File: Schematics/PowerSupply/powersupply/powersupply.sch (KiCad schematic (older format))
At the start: 12 parts, among them J1 +/- 15V Regulated, J2 +/- 18V unregulated, T1 Transformer_1P_2S, U1 L7815, U2 L7915

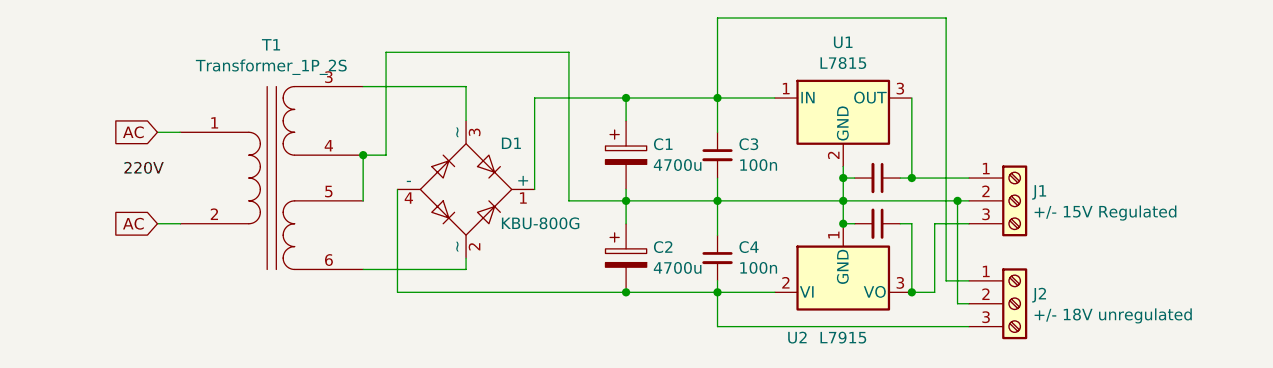
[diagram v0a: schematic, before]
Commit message: Create PCB for the power supply (amp)
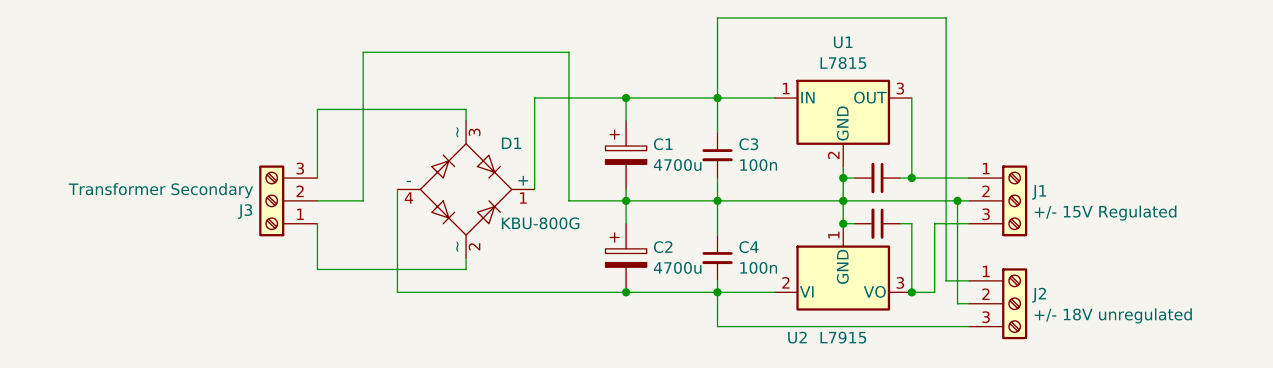
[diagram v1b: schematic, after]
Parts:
- removed T1: Transformer_1P_2S, symbol Device:Transformer_1P_2S
- added J3: Transformer Secondary, TerminalBlock:TerminalBlock_Altech_AK300-3_P5.00mm, symbol Connector:Screw_Terminal_01x03
- C1, C2: footprint (none) -> Capacitor_THT:CP_Radial_D10.0mm_P5.00mm
- C3, C4, C5, C6: footprint (none) -> Capacitor_THT:C_Rect_L4.0mm_W2.5mm_P2.50mm
- J1, J2: footprint (none) -> TerminalBlock:TerminalBlock_Altech_AK300-3_P5.00mm
- U1, U2: footprint (none) -> Package_TO_SOT_THT:TO-220-3_Vertical
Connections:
- net at D1.2 (~~): now also J3.1 (Pin_1)
- net at D1.3 (~~): now also J3.3 (Pin_3)
- net at C1.2, C2.1, C3.2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: now also J3.2 (Pin_2)
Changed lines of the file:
@@
 EESchema Schematic File Version 4
-EELAYER 30 0
+LIBS:powersupply-cache
+EELAYER 29 0
 EELAYER END
 $Descr A4 11693 8268
@@
 F 0 "C1" H 5318 3996 50  0000 L CNN
 F 1 "4700u" H 5318 3905 50  0000 L CNN
-F 2 "" H 5238 3800 50  0001 C CNN
+F 2 "Capacitor_THT:CP_Radial_D10.0mm_P5.00mm" H 5238 3800 50  0001 C CNN
 F 3 "~" H 5200 3950 50  0001 C CNN
 	1    5200 3950
@@
 F 0 "C2" H 5318 4446 50  0000 L CNN
 F 1 "4700u" H 5318 4355 50  0000 L CNN
-F 2 "" H 5238 4250 50  0001 C CNN
+F 2 "Capacitor_THT:CP_Radial_D10.0mm_P5.00mm" H 5238 4250 50  0001 C CNN
 F 3 "~" H 5200 4400 50  0001 C CNN
 	1    5200 4400
@@
 F 0 "C3" H 5692 3996 50  0000 L CNN
 F 1 "100n" H 5692 3905 50  0000 L CNN
-F 2 "" H 5600 3950 50  0001 C CNN
+F 2 "Capacitor_THT:C_Rect_L4.0mm_W2.5mm_P2.50mm" H 5600 3950 50  0001 C CNN
 F 3 "~" H 5600 3950 50  0001 C CNN
 	1    5600 3950
@@
 F 0 "C4" H 5692 4446 50  0000 L CNN
 F 1 "100n" H 5692 4355 50  0000 L CNN
-F 2 "" H 5600 4400 50  0001 C CNN
+F 2 "Capacitor_THT:C_Rect_L4.0mm_W2.5mm_P2.50mm" H 5600 4400 50  0001 C CNN
 F 3 "~" H 5600 4400 50  0001 C CNN
 	1    5600 4400
@@
 	4200 4550 5200 4550
 Connection ~ 5200 4550
-$Comp
-L Device:Transformer_1P_2S T1
-U 1 1 5E2C33F1
-P 3650 4050
-F 0 "T1" H 3650 4631 50  0000 C CNN
-F 1 "Transformer_1P_2S" H 3650 4540 50  0000 C CNN
-F 2 "" H 3650 4050 50  0001 C CNN
-F 3 "~" H 3650 4050 50  0001 C CNN
-	1    3650 4050
-	1    0    0    -1
-$EndComp
 Wire Wire Line
 	4950 4150 5200 4150
 Wire Wire Line
-	4050 4450 4500 4450
-Wire Wire Line
 	4500 4450 4500 4400
 Wire Wire Line
-	4050 3650 4500 3650
-Wire Wire Line
-	4500 3650 4500 3800
-Text GLabel 3150 3850 0    50   Input ~ 0
-AC
-Wire Wire Line
-	3150 3850 3250 3850
-Text GLabel 3150 4250 0    50   Input ~ 0
-AC
-Wire Wire Line
-	3150 4250 3250 4250
-Wire Wire Line
-	4950 3500 4150 3500
-Wire Wire Line
-	4150 3500 4150 3950
-Wire Wire Line
-	4150 3950 4050 3950
+	4500 3750 4500 3800
 Wire Wire Line
 	4950 3500 4950 4150
 Wire Wire Line
-	4050 4150 4050 3950
-Connection ~ 4050 3950
+	4050 4150 4050 3500
 $Comp
 L Regulator_Linear:L7815 U1
@@
 F 0 "U1" H 6150 3942 50  0000 C CNN
 F 1 "L7815" H 6150 3851 50  0000 C CNN
-F 2 "" H 6175 3550 50  0001 L CIN
+F 2 "Package_TO_SOT_THT:TO-220-3_Vertical" H 6175 3550 50  0001 L CIN
 F 3 "http://www.st.com/content/ccc/resource/technical/document/datasheet/41/4f/b3/b0/12/d4/47/88/CD00000444.pdf/files/CD00000444.pdf/jcr:content/translations/en.CD00000444.pdf" H 6150 3650 50  0001 C CNN
 	1    6150 3700
@@
 F 0 "U2" H 5950 4350 50  0000 C CNN
 F 1 "L7915" H 6150 4350 50  0000 C CNN
-F 2 "" H 6150 4350 50  0001 C CIN
+F 2 "Package_TO_SOT_THT:TO-220-3_Vertical" H 6150 4350 50  0001 C CIN
 F 3 "http://www.st.com/content/ccc/resource/technical/document/datasheet/c9/16/86/41/c7/2b/45/f2/CD00000450.pdf/files/CD00000450.pdf/jcr:content/translations/en.CD00000450.pdf" H 6150 4550 50  0001 C CNN
 	1    6150 4550
@@
 F 0 "J1" H 6980 4192 50  0000 L CNN
 F 1 "+/- 15V Regulated" H 6980 4101 50  0000 L CNN
-F 2 "" H 6900 4150 50  0001 C CNN
+F 2 "TerminalBlock:TerminalBlock_Altech_AK300-3_P5.00mm" H 6900 4150 50  0001 C CNN
 F 3 "~" H 6900 4150 50  0001 C CNN
 	1    6900 4150
@@
 F 0 "J2" H 6980 4642 50  0000 L CNN
 F 1 "+/- 18V unregulated" H 6980 4551 50  0000 L CNN
-F 2 "" H 6900 4600 50  0001 C CNN
+F 2 "TerminalBlock:TerminalBlock_Altech_AK300-3_P5.00mm" H 6900 4600 50  0001 C CNN
 F 3 "~" H 6900 4600 50  0001 C CNN
 	1    6900 4600
@@
 F 0 "C5" V 6071 4050 50  0001 C CNN
 F 1 "C_Small" V 6162 4050 50  0001 C CNN
-F 2 "" H 6300 4050 50  0001 C CNN
+F 2 "Capacitor_THT:C_Rect_L4.0mm_W2.5mm_P2.50mm" H 6300 4050 50  0001 C CNN
 F 3 "~" H 6300 4050 50  0001 C CNN
 	1    6300 4050
@@
 F 0 "C6" V 6071 4250 50  0001 C CNN
 F 1 "C_Small" V 6163 4250 50  0001 C CNN
-F 2 "" H 6300 4250 50  0001 C CNN
+F 2 "Capacitor_THT:C_Rect_L4.0mm_W2.5mm_P2.50mm" H 6300 4250 50  0001 C CNN
 F 3 "~" H 6300 4250 50  0001 C CNN
 	1    6300 4250
@@
 	6200 4250 6150 4250
 Connection ~ 6150 4250
-Text Label 3000 4050 0    50   ~ 0
-220V
 Wire Wire Line
 	6450 4550 6550 4550
@@
 Wire Wire Line
 	6650 4150 6700 4150
+$Comp
+L Connector:Screw_Terminal_01x03 J3
+U 1 1 5E3BE712
+P 3650 4150
+F 0 "J3" H 3730 4192 50  0000 L CNN
+F 1 "Transformer Secondary" H 3730 4101 50  0000 L CNN
+F 2 "TerminalBlock:TerminalBlock_Altech_AK300-3_P5.00mm" H 3650 4150 50  0001 C CNN
+F 3 "~" H 3650 4150 50  0001 C CNN
+	1    3650 4150
+	-1   0    0    1
+$EndComp
+Wire Wire Line
+	3850 4450 3850 4250
+Wire Wire Line
+	3850 4450 4500 4450
+Wire Wire Line
+	3850 3750 3850 4050
+Wire Wire Line
+	3850 3750 4500 3750
+Wire Wire Line
+	4050 4150 3850 4150
+Wire Wire Line
+	4050 3500 4950 3500
 $EndSCHEMATC

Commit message: Add final version of the powersupply pcb
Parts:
- C1, C2: footprint Capacitor_THT:CP_Radial_D10.0mm_P5.00mm -> Capacitor_THT:CP_Radial_D17.0mm_P7.50mm
- C3, C4, C5, C6: footprint Capacitor_THT:C_Rect_L4.0mm_W2.5mm_P2.50mm -> Capacitor_THT:C_Rect_L9.0mm_W2.5mm_P7.50mm_MKT
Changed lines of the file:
@@
 F 0 "C1" H 5318 3996 50  0000 L CNN
 F 1 "4700u" H 5318 3905 50  0000 L CNN
-F 2 "Capacitor_THT:CP_Radial_D10.0mm_P5.00mm" H 5238 3800 50  0001 C CNN
+F 2 "Capacitor_THT:CP_Radial_D17.0mm_P7.50mm" H 5238 3800 50  0001 C CNN
 F 3 "~" H 5200 3950 50  0001 C CNN
 	1    5200 3950
@@
 F 0 "C2" H 5318 4446 50  0000 L CNN
 F 1 "4700u" H 5318 4355 50  0000 L CNN
-F 2 "Capacitor_THT:CP_Radial_D10.0mm_P5.00mm" H 5238 4250 50  0001 C CNN
+F 2 "Capacitor_THT:CP_Radial_D17.0mm_P7.50mm" H 5238 4250 50  0001 C CNN
 F 3 "~" H 5200 4400 50  0001 C CNN
 	1    5200 4400
@@
 F 0 "C3" H 5692 3996 50  0000 L CNN
 F 1 "100n" H 5692 3905 50  0000 L CNN
-F 2 "Capacitor_THT:C_Rect_L4.0mm_W2.5mm_P2.50mm" H 5600 3950 50  0001 C CNN
+F 2 "Capacitor_THT:C_Rect_L9.0mm_W2.5mm_P7.50mm_MKT" H 5600 3950 50  0001 C CNN
 F 3 "~" H 5600 3950 50  0001 C CNN
 	1    5600 3950
@@
 F 0 "C4" H 5692 4446 50  0000 L CNN
 F 1 "100n" H 5692 4355 50  0000 L CNN
-F 2 "Capacitor_THT:C_Rect_L4.0mm_W2.5mm_P2.50mm" H 5600 4400 50  0001 C CNN
+F 2 "Capacitor_THT:C_Rect_L9.0mm_W2.5mm_P7.50mm_MKT" H 5600 4400 50  0001 C CNN
 F 3 "~" H 5600 4400 50  0001 C CNN
 	1    5600 4400
@@
 F 0 "C5" V 6071 4050 50  0001 C CNN
 F 1 "C_Small" V 6162 4050 50  0001 C CNN
-F 2 "Capacitor_THT:C_Rect_L4.0mm_W2.5mm_P2.50mm" H 6300 4050 50  0001 C CNN
+F 2 "Capacitor_THT:C_Rect_L9.0mm_W2.5mm_P7.50mm_MKT" H 6300 4050 50  0001 C CNN
 F 3 "~" H 6300 4050 50  0001 C CNN
 	1    6300 4050
@@
 F 0 "C6" V 6071 4250 50  0001 C CNN
 F 1 "C_Small" V 6163 4250 50  0001 C CNN
-F 2 "Capacitor_THT:C_Rect_L4.0mm_W2.5mm_P2.50mm" H 6300 4250 50  0001 C CNN
+F 2 "Capacitor_THT:C_Rect_L9.0mm_W2.5mm_P7.50mm_MKT" H 6300 4250 50  0001 C CNN
 F 3 "~" H 6300 4250 50  0001 C CNN
 	1    6300 4250
